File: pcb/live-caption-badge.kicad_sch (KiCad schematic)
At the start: 15 parts, among them J1 USB_C_Receptacle_USB2.0_14P, J2 Conn_01x24_Socket, J3 AudioJack4, SW1 SW_SPDT, U1 ESP32-S3-WROOM-1, U2 HE9073A33M5R

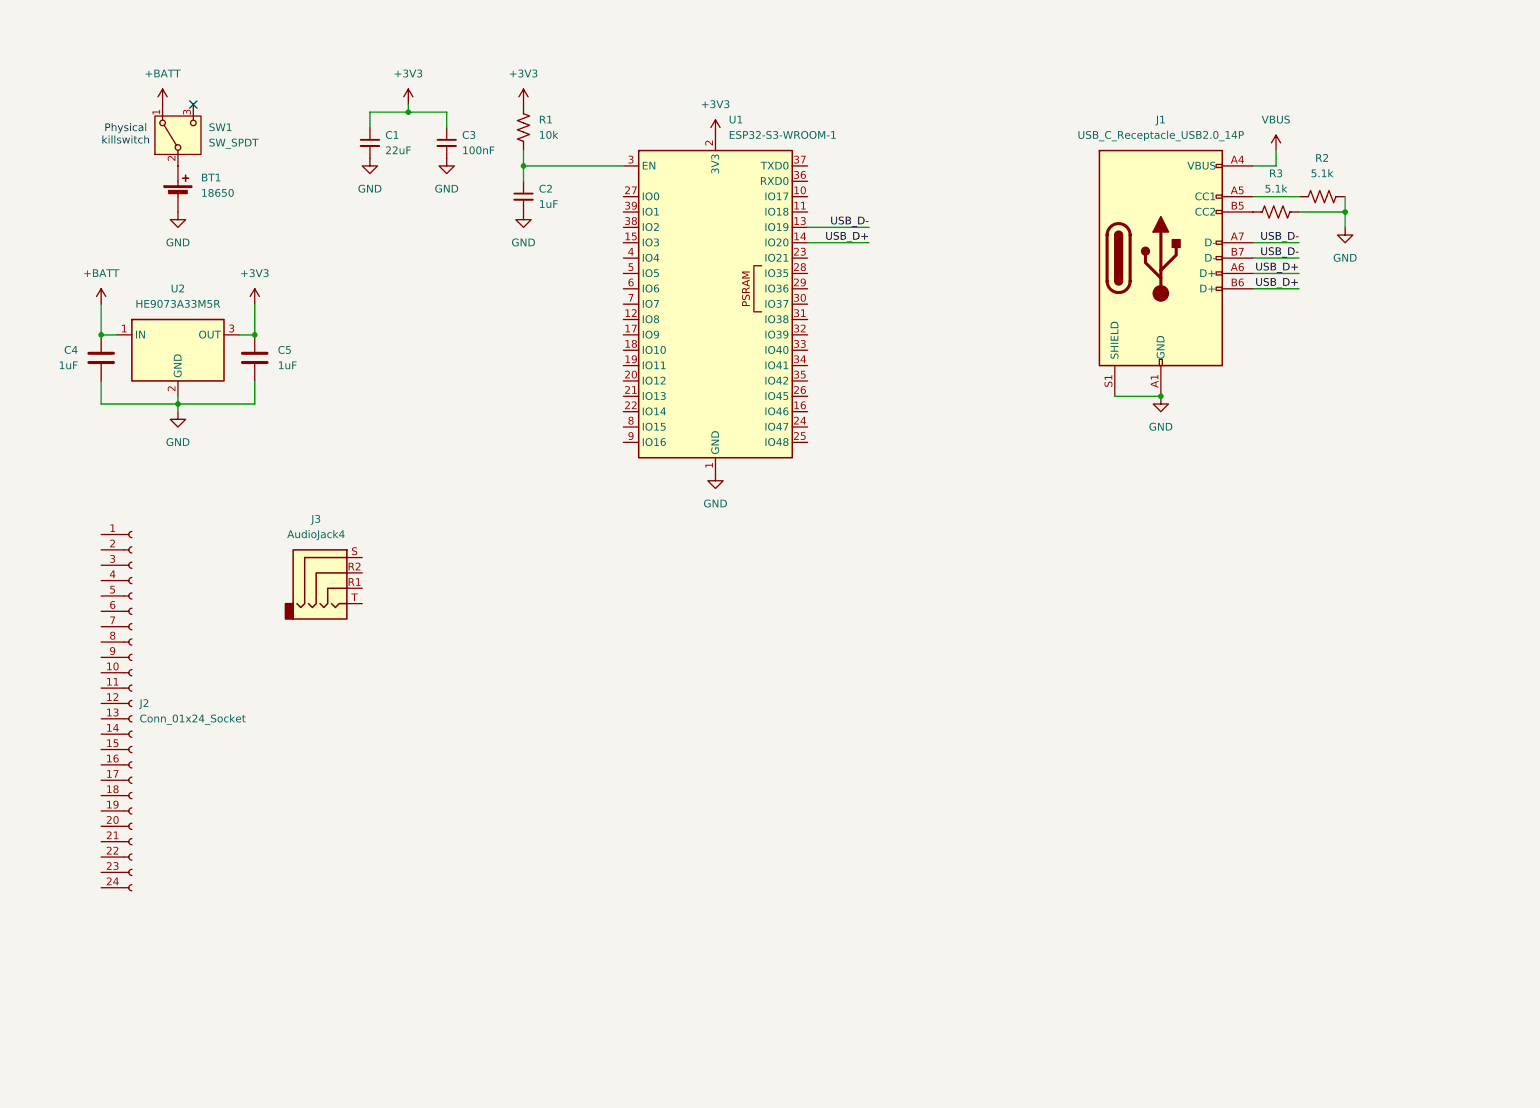
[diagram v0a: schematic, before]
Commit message: pcb: Add ES7210
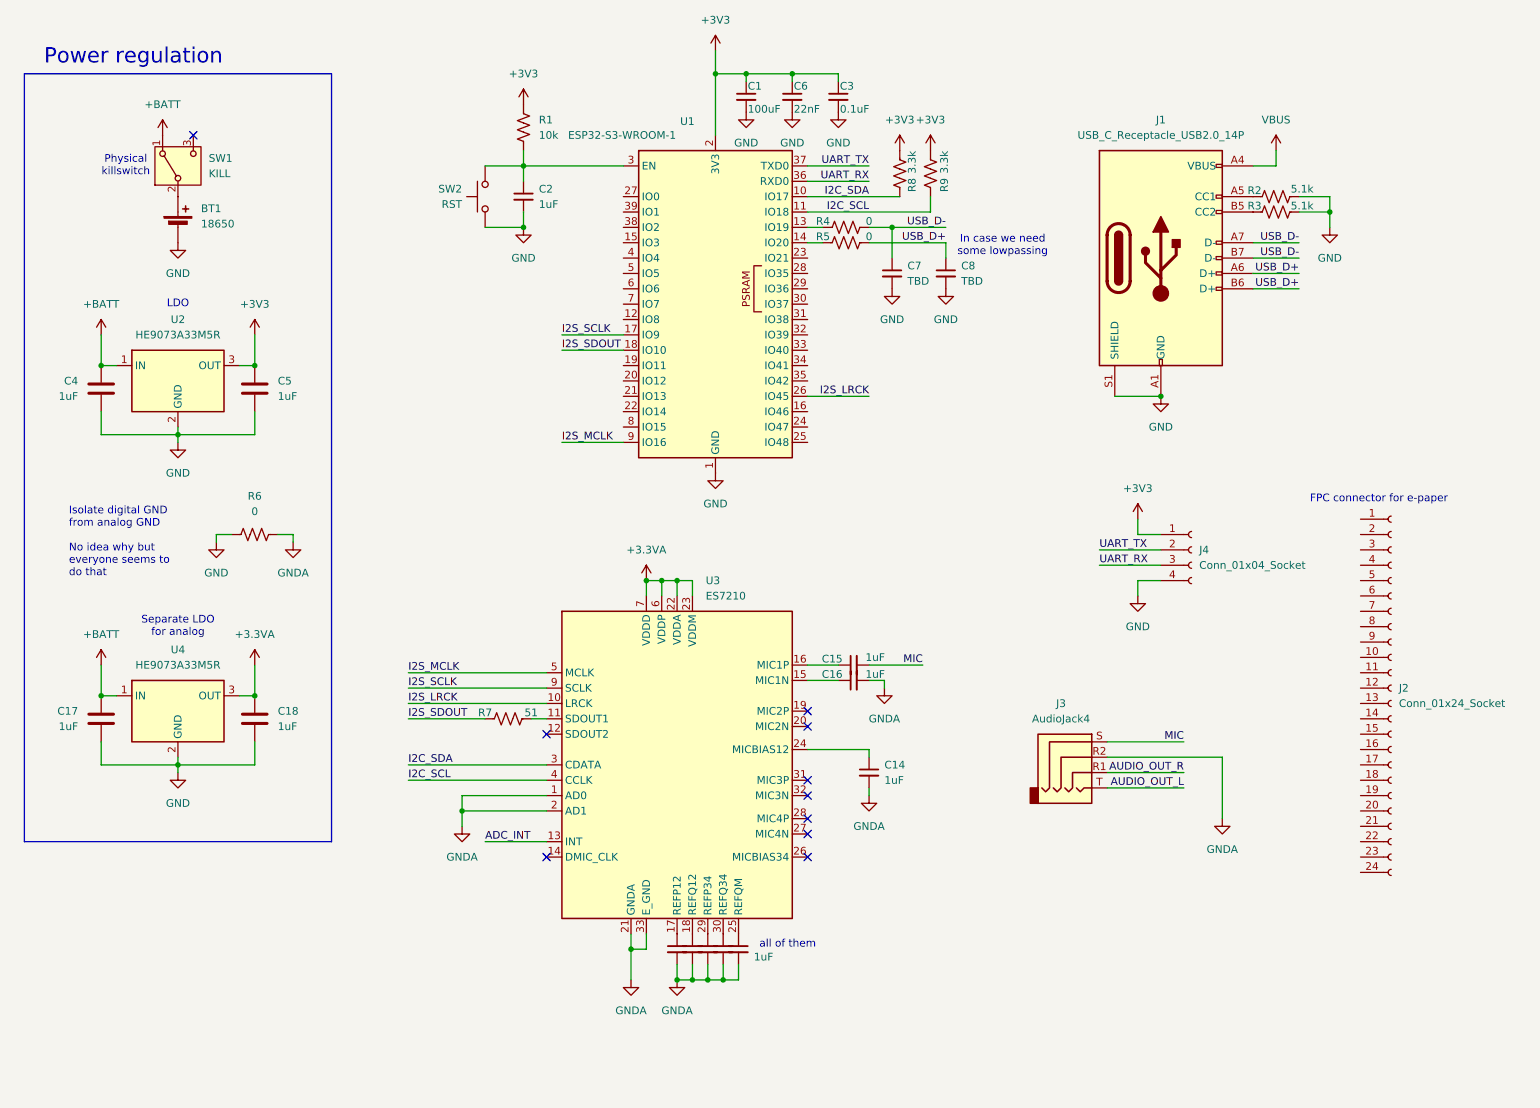
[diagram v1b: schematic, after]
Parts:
- added C10, C11, C12, C13, C14, C15, C16, C9: 1uF, symbol Device:C_Small
- added C17, C18: 1uF, symbol Device:C
- added C6: 22nF, symbol Device:C_Small
- added C7, C8: TBD, symbol Device:C_Small
- added J4: Conn_01x04_Socket, symbol Connector:Conn_01x04_Socket
- added R4, R5, R6: 0, symbol Device:R_US
- added R7: 51, symbol Device:R_US
- added R8, R9: 3.3k, symbol Device:R_US
- added SW2: RST, symbol Switch:SW_Push
- added U3: ES7210, symbol live-caption-badge:ES7210
- added U4: HE9073A33M5R, symbol Regulator_Linear:LT1963AxST-3.3
- C1: value 22uF -> 100uF
- C3: value 100nF -> 0.1uF
- SW1: value SW_SPDT -> KILL
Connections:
- net +3V3: now also C6.1, J4.1 (Pin_1), R8.1, R9.1
- net +BATT: now also C17.1, U4.1 (IN)
- net GND: now also C17.2, C18.2, C6.2, C7.2, C8.2, J4.4 (Pin_4), R6.1, SW2.1, U4.2 (GND)
- net USB_D+: now also C8.1, R5.2; no longer U1.14 (IO20)
- net USB_D-: now also C7.1, R4.2; no longer U1.13 (IO19)
- net at C2.1, R1.2, U1.3 (EN): now also SW2.2
- net I2C_SDA: now reaches U1.10 (IO17)
- net I2C_SDA: now also R8.2, U3.3 (CDATA)
- net I2C_SCL: now reaches U1.11 (IO18)
- net I2C_SCL: now also R9.2, U3.4 (CCLK)
- net I2S_SCLK: now reaches U1.17 (IO9)
- net I2S_SCLK: now also U3.9 (SCLK)
- net I2S_SDOUT: now reaches U1.18 (IO10)
- net I2S_SDOUT: now also R7.1
- net I2S_LRCK: now reaches U1.26 (IO45)
- net I2S_LRCK: now also U3.10 (LRCK)
- net UART_RX: now reaches U1.36 (RXD0)
- net UART_RX: now also J4.3 (Pin_3)
- net UART_TX: now reaches U1.37 (TXD0)
- net UART_TX: now also J4.2 (Pin_2)
- net I2S_MCLK: now reaches U1.9 (IO16)
- net I2S_MCLK: now also U3.5 (MCLK)
- net AUDIO_OUT_R: now reaches J3.R1
- net GNDA: now reaches J3.R2
- net GNDA: now also C10.2, C11.2, C12.2, C13.2, C14.2, C16.2, C9.2, R6.2, U3.1 (AD0), U3.2 (AD1), U3.21 (GNDA), U3.33 (E_GND)
- net MIC: now reaches J3.S
- net MIC: now also C15.2
- net AUDIO_OUT_L: now reaches J3.T
- new net: C14.1, U3.24 (MICBIAS12)
- new net: C10.1, U3.18 (REFQ12)
- new net: C13.1, U3.25 (REFQM)
- new net: C11.1, U3.29 (REFP34)
- new net: R7.2, U3.11 (SDOUT1)
- new net: C16.1, U3.15 (MIC1N)
- new net: C15.1, U3.16 (MIC1P)
- new net: C9.1, U3.17 (REFP12)
- new net: C12.1, U3.30 (REFQ34)
- new net: R4.1, U1.13 (IO19)
- new net: R5.1, U1.14 (IO20)
- new net +3.3VA: C18.1, U3.22 (VDDA), U3.23 (VDDM), U3.6 (VDDP), U3.7 (VDDD), U4.3 (OUT)
- new net ADC_INT: U3.13 (INT)
- no-connect marks 1 -> 10
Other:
- note added: "FPC connector for e-paper"
- note added: "In case we need some lowpassing"
- note added: "Isolate digital GND from analog GND No idea why but everyone seems to do that"
- note added: "LDO"
- note added: "Power regulation"
- note added: "Separate LDO for analog"
- note added: "all of them"
- moved on the sheet: BT1, C1, C3, C4, C5, J2, J3, R2, SW1, U2

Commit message: pcb: moved things around
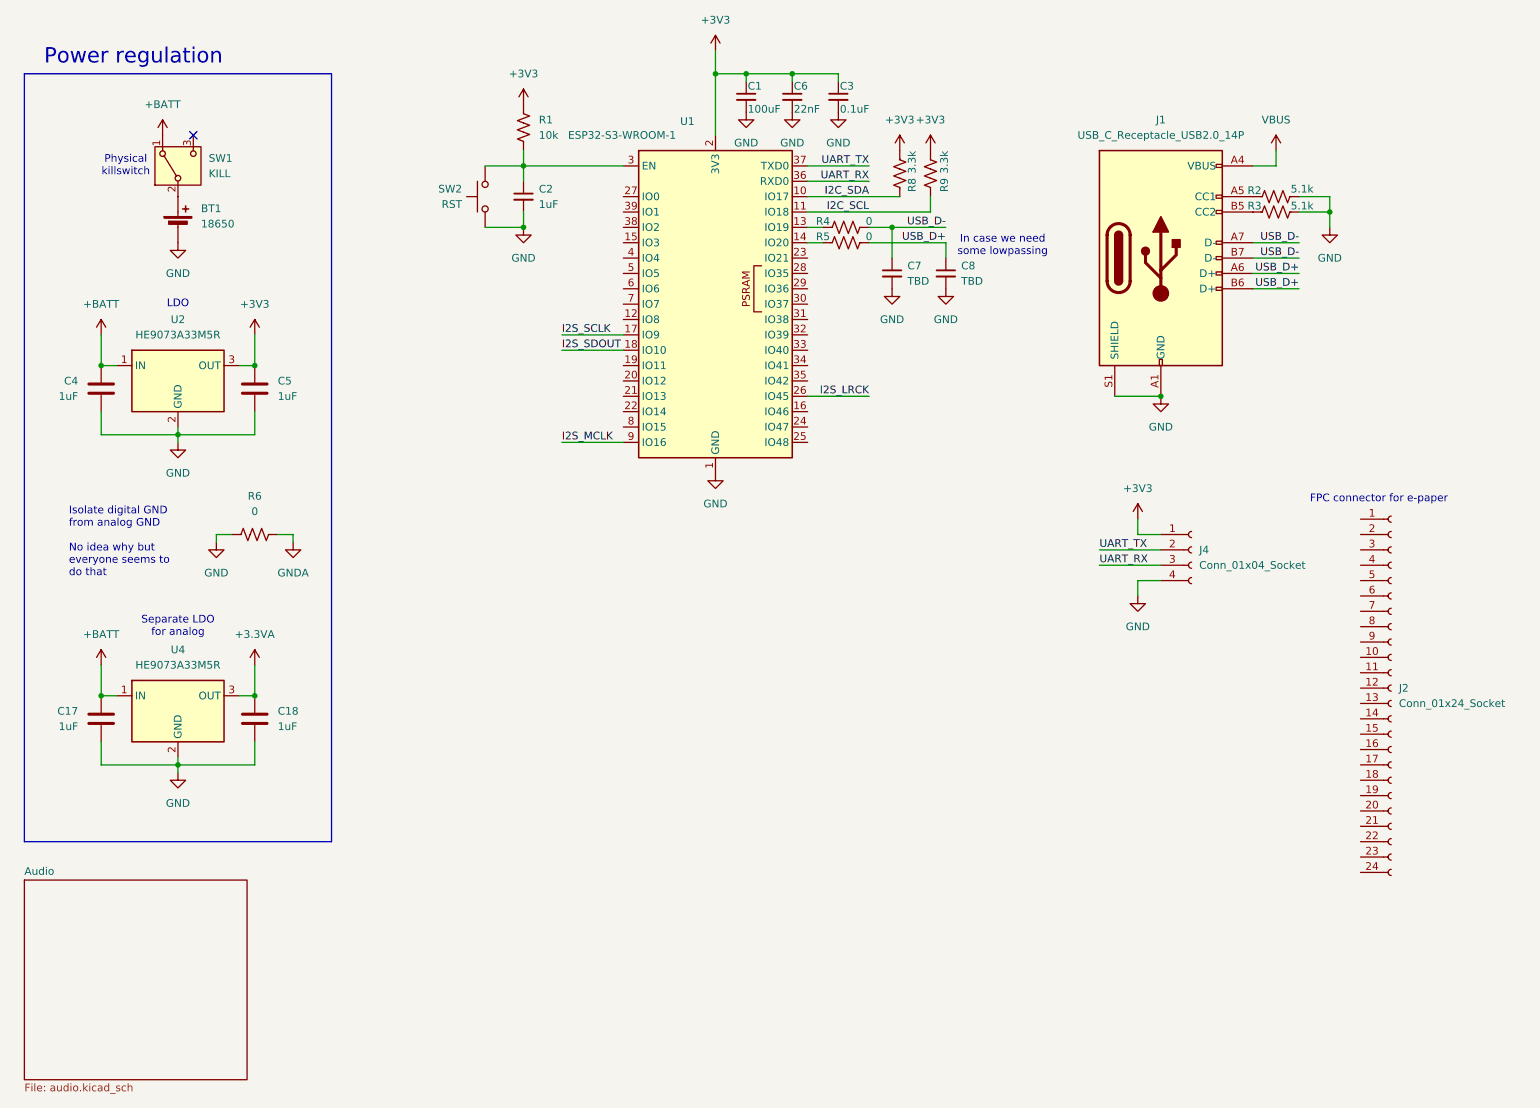
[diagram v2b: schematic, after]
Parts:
- removed C10, C11, C12, C13, C14, C15, C16, C9: 1uF, symbol Device:C_Small
- removed J3: AudioJack4, symbol Connector_Audio:AudioJack4
- removed R7: 51, symbol Device:R_US
- removed U3: ES7210, symbol live-caption-badge:ES7210
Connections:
- no-connect marks 10 -> 1
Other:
- added sheet Audio (audio.kicad_sch)
- note removed: "all of them"

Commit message: epaper driver schematic
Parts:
- removed J2: Conn_01x24_Socket, symbol Connector:Conn_01x24_Socket
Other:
- added sheet Epaper_Driver (epaper_driver.kicad_sch)
- note removed: "FPC connector for e-paper"
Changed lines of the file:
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@@
 		)
 	)
-	(text "FPC connector for e-paper"
-		(exclude_from_sim no)
-		(at 249.428 95.758 0)
-		(effects
-			(font
-				(size 1.27 1.27)
-			)
-		)
-	)
 	(text "Power regulation"
 		(exclude_from_sim no)
@@
 	)
 	(symbol
-		(lib_id "Connector:Conn_01x24_Socket")
-		(at 251.46 127 0)
-		(unit 1)
-		(exclude_from_sim no)
-		(in_bom yes)
-		(on_board yes)
-		(dnp no)
-		(fields_autoplaced yes)
-		(property "Reference" "J2"
-			(at 252.73 126.9999 0)
-			(effects
-				(font
-					(size 1.27 1.27)
-				)
-				(justify left)
-			)
-		)
-		(property "Value" "Conn_01x24_Socket"
-			(at 252.73 129.5399 0)
-			(effects
-				(font
-					(size 1.27 1.27)
-				)
-				(justify left)
-			)
-		)
-		(property "Footprint" ""
-			(at 251.46 127 0)
-			(effects
-				(font
-					(size 1.27 1.27)
-				)
-				(hide yes)
-			)
-		)
-		(property "Datasheet" "~"
-			(at 251.46 127 0)
-			(effects
-				(font
-					(size 1.27 1.27)
-				)
-				(hide yes)
-			)
-		)
-		(property "Description" "Generic connector, single row, 01x24, script generated"
-			(at 251.46 127 0)
-			(effects
-				(font
-					(size 1.27 1.27)
-				)
-				(hide yes)
-			)
-		)
-		(pin "24"
-		)
-		(pin "17"
-		)
-		(pin "21"
-		)
-		(pin "3"
-		)
-		(pin "23"
-		)
-		(pin "2"
-		)
-		(pin "20"
-		)
-		(pin "19"
-		)
-		(pin "6"
-		)
-		(pin "5"
-		)
-		(pin "7"
-		)
-		(pin "4"
-		)
-		(pin "9"
-		)
-		(pin "8"
-		)
-		(pin "14"
-		)
-		(pin "18"
-		)
-		(pin "11"
-		)
-		(pin "16"
-		)
-		(pin "22"
-		)
-		(pin "15"
-		)
-		(pin "12"
-		)
-		(pin "13"
-		)
-		(pin "10"
-		)
-		(pin "1"
-		)
-		(instances
-			(project ""
-				(path "/3b930924-1452-4d23-815e-09afbcdc5905"
-					(reference "J2")
-					(unit 1)
-				)
-			)
-		)
-	)
-	(symbol
 		(lib_id "Device:C")
 		(at 38.1 77.47 0)
@@
 				)
 			)
+		)
+	)
+	(sheet
+		(at 114.3 113.03)
+		(size 15.24 31.75)
+		(fields_autoplaced yes)
+		(stroke
+			(width 0.1524)
+			(type solid)
+		)
+		(fill
+			(color 0 0 0 0.0000)
+		)
+		(property "Sheetname" "Epaper_Driver"
+			(at 114.3 112.3184 0)
+			(effects
+				(font
+					(size 1.27 1.27)
+				)
+				(justify left bottom)
+			)
+		)
+		(property "Sheetfile" "epaper_driver.kicad_sch"
+			(at 114.3 145.3646 0)
+			(effects
+				(font
+					(size 1.27 1.27)
+				)
+				(justify left top)
+			)
+		)
+		(instances
+			(project "live-caption-badge"
+				(path "/3b930924-1452-4d23-815e-09afbcdc5905"
+					(page "3")
+				)
+			)
